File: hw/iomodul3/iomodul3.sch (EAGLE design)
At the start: 56 parts, among them IC1 MCP2551, IC3 STM32F042K, IC4 MCP1700T3302E/TT, IC5 DS8289, Q2 8MHz

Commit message: board version 3 begonnen
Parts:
- removed C10: 1µ 6,3V, schlager_passiv:C-EUC0805
- removed C11, C5: 12p, schlager_passiv:C-EUC0805
- removed C4: (no value), schlager_passiv:C-EUC0805
- removed C6: 10n, schlager_passiv:C-EUC0805
- removed C7, C9: 4µ7 6,3V, schlager_passiv:C-EUC0805
- removed C8: 100n, schlager_passiv:C-EUC0805
- removed IC3: STM32F042K, MYSGS:STM32F042
- removed JP3: (no value), pinhead:PINHD-1X6
- removed Q1: (no value), crystal:CRYSTALHC49U-V
- removed Q2: 8MHz, MYPASS:MT-CRYSTAL
- removed R4, R6, R9: (no value), schlager_passiv:R-EU_R0805
- added C20: 1uF, schlager_passiv:C-EUC0805
- added C21, C22, C26, C27: 100nF, schlager_passiv:C-EUC0805
- added C23, C24: 22p, schlager_passiv:C-EUC0805
- added CN2: PINHEAD-2x5-P1.27, Connettori:0171_PH127-205DF055G00A
- added IC2: SAMD21G18A-AUT, IntegratedCircuits:1792_SAMD21G18A-AUT
- added ICSP: 3x2 M, Connettori:0114_PH254-203DF118A00V
- added L6, L7: MH2029-300Y, Protezione:0001_BLM21PG300SN1D_/_MH2029-300Y
- added R15: 10k, schlager_passiv:R-EU_R0805
- added R18: 330R, schlager_passiv:R-EU_R0805
- added U$1: MCP2515-I/ST, CHIP_MCP:MCP2515-I/ST
- added USB2: MICRO-USB-AB1, Connettori:0631_MCR-AB1-S-RA-SMT-TR
- added Y1, Y4: 32,768Khz_SMD, Cristalli:0213_ABS07-32.768KHZ-T
- added Z5, Z6: CG0603MLC-05E, Protezione:0010_BRNCG0603MLC-05E
- C2, C3: value 100n -> 22p
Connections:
- removed net LED1: IC3G$1.PA5/AIN5, R5.2
- removed net N$5: C5.2, IC3G$1.PF0/OSC_IN, Q1.2, Q2G$1.2
- removed net NRST: IC3G$1./RST, JP3.5
- removed net PA1: IC3G$1.PA1/AIN1, SV1.5
- removed net PA10: IC3G$1.PA10, SV1.11
- removed net PA15: IC3G$1.PA15, SV1.12
- removed net PA2: IC3G$1.PA2/AIN2, SV1.6
- removed net PA3: IC3G$1.PA3/AIN3, SV1.18
- removed net PA6: IC3G$1.PA6/AIN6, SV1.7
- removed net PA7: IC3G$1.PA7/AIN7, SV1.8
- removed net PA8: IC3G$1.PA8, SV1.9
- removed net PA9: IC3G$1.PA9, SV1.10
- removed net PB3: IC3G$1.PB3/SPI1_SCK, SV1.13
- removed net PB4: IC3G$1.PB4/SPI1_MISO, SV1.14
- removed net PB5: IC3G$1.PB5/SPI1_MOSI, SV1.15
- removed net PB6: IC3G$1.PB6/I2C1_SCL, SV1.16
- removed net PB7: IC3G$1.PB7/I2C1_SDA, SV1.17
- removed net SWCLK: IC3G$1.PA14, JP3.2
- removed net SWDIO: IC3G$1.PA13, JP3.4
- removed net SWO: JP3.6
- removed net UIN: C4.1, IC3G$1.PA0/AIN0, R4.2, R6.1
- removed net VDD_TARGET: JP3.1
- new net #0_RX: IC2.PB23/EIC/SCOM5PAD3, SV1.17
- new net #11_MOSI: IC2.PA16/I2C/EIC/SCOM1PAD0+/TC2, SV1.15, U$1.SI
- new net #12_MISO: IC2.PA19/EIC/SCOM1PAD3+/TC3, SV1.14, U$1.SO
- new net #13_SCK: IC2.PA17/I2C/EIC/SCOM1PAD1+/TC2, SV1.13, U$1.SCK
- new net #1_TX: IC2.PB22/EIC/SCOM5PAD2, SV1.16
- new net #3_IO: IC2.PA9/I2C/EIC/AIN17/SCOM2PAD1+/TC0, SV1.9
- new net #9_CS_HEADER: IC2.PA7/EIC/AIN7/SCOM0PAD3/TC1, SV1.12
- new net #A0: IC2.PA2/EIC/AIN0, SV1.5
- new net #A1: IC2.PB8/EIC/AIN2/SCOM4PAD0/TC4, SV1.6
- new net #A2: IC2.PB9/EIC/AIN3/SCOM4PAD1//TC4, SV1.7
- new net #A3: IC2.PA4/EIC/REF/AIN4/SCOM0PAD0/TC0, SV1.8
- new net #A4: IC2.PA5/EIC/AIN5/SCOM0PAD1/TC0, SV1.18
- new net CS_MCP: IC2.PA18/EIC/SCOM1PAD2+/TC3, U$1.~CS
- new net DGI_GPIO0: IC2.PA13/I2C/EIC/SCOM2PAD1+/TC2
- new net DGI_GPIO1: IC2.PA21/EIC/SCOM5PAD3+
- new net DGI_GPIO2: IC2.PA6/EIC/AIN6/SCOM0PAD2/TC1
- new net MCPOSC1: C3.1, U$1.OSC1, Y1.1
- new net MCPOSC2: C2.1, U$1.OSC2, Y1.2
- new net PA00_XIN32: C23.2, IC2.PA0/XIN32/EIC/SCOM1PAD0/TC2, Y4.2
- new net PA01_XOUT32: C24.2, IC2.PA1/XOUT32/EIC/SCOM1PAD1/TC2, Y4.1
- new net PA03_AREFA: IC2.PA3/EIC/REF/AIN1
- new net PA08_TCC0-W0: IC2.PA8/I2C/AIN16/SCOM2PAD0+/TC0
- new net PA10_TCC0-W2: IC2.PA10/EIC/AIN18/SCOM2PAD2+/TC1
- new net PA11_TCC0-W3: IC2.PA11/EIC/AIN19/SCOM2PAD3+/TC1
- new net PA14_TCC0-W4: IC2.PA14/XIN/EIC/SCOM2PAD2+/TC3
- new net PA15_TCC0-W5: IC2.PA15/XOUT/EIC/SCOM2PAD3+/TC3
- new net PA20_TCC0-W6: IC2.PA20/EIC/SCOM5PAD2+
- new net PA27_TX_LED: IC2.PA27/EIC
- new net PA28_USB_HOST_EN: IC2.PA28/EIC
- new net PA30_SWCLK: CN2.4, IC2.PA30/EIC/SCOM1PAD2/TC1
- new net PA31_SWDIO1: CN2.2, IC2.PA31/EIC/SCOM1PAD3/TC1
- new net PB02_AIN10: IC2.PB2/EIC/AIN10/SCOM5PAD0
- new net PB03_RX_LED: IC2.PB3/EIC/AIN11/SCOM5PAD1
- new net PB10_S4_SPI_MOSI: IC2.PB10/EIC/SCOM4PAD2/TC5, ICSP.4
- new net PB11_S4_SPI_SCK: IC2.PB11/EIC/SCOM4PAD3/TC5, ICSP.3
- new net PB12_S4_SPI_MISO: IC2.PA12/I2C/EIC/SCOM2PAD0+/TC2, ICSP.1
- new net RESET: CN2.10, ICSP.5, R18.2
- new net SCL: IC2.PA23/I2C/EIC/SCOM5PAD1+/TC4, R2.1, SV1.10
- new net SDA: IC2.PA22/I2C/EIC/SCOM5PAD0+/TC4, R15.1, SV1.11
- new net TARGET_RESET_EDBG: IC2.RESETN, R18.1, U$1.~RESET
- new net TARGET_USB_N: IC2.PA24/EIC/SCOM3PAD2+/TC5, USB2.D-, Z6.1
- new net TARGET_USB_P: IC2.PA25/EIC/SCOM3PAD3+/TC5, USB2.D+, Z5.1
- new net VDDCORE: C20.1, IC2.VDDCORE1
- net +24V: no longer R4.1
- net +3V3: now also C21.1, C26.1, C27.2, CN2.1, IC2.VDDIN, IC2.VDDIO1, IC2.VDDIO2, L6.2, R15.2, R2.2; no longer C10.2, C2.2, C3.2, C6.2, C7.2, C9.2, IC3G$2.VCC, IC3G$2.VCC1, IC3G$2.VCCA
- net +5V: now also ICSP.2
- net CANRX: now also U$1.RXCAN; no longer IC3G$1.PA11/CAN_RX
- net CANTX: now also U$1.TXCAN; no longer IC3G$1.PA12/CAN_TX
- net GND: now also C2.2, C20.2, C21.2, C22.2, C23.1, C24.1, C26.2, C27.1, C3.2, CN2.3, CN2.5, CN2.9, IC2.GND1, IC2.GND2, IC2.GND3, IC2.GNDANA, ICSP.6, L7.2, USB2.UGND, Z5.2, Z6.2; no longer C10.1, C11.1, C2.1, C3.1, C4.2, C5.1, C6.1, C7.1, C8.2, C9.1, IC3G$2.GND, IC3G$2.GND1, JP3.3, Q2G$2.GND, Q2G$3.GND, R2.2, R6.2, R9.2
- net LED2: no longer IC3G$1.PA4/AIN4
- net LED3_: no longer IC3G$1.PB0/AIN8
- net LED4_: no longer IC3G$1.BP1/AIN9
- net N$15: now also C22.1, IC2.VDDANA, L6.1; no longer IC3G$1.PB8/BOOT0, R2.1
- net N$4: now also L7.1, USB2.G1, USB2.G10, USB2.G11, USB2.G2, USB2.G3, USB2.G4, USB2.G5, USB2.G6, USB2.G7, USB2.G8, USB2.G9, USB2.SH1, USB2.SH2, USB2.SH3, USB2.SH4; no longer C11.2, IC3G$1.PF1/OSC_OUT, Q1.1, Q2G$1.1
- net PE: no longer C8.1, CON2G$2.FGND, R9.1
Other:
- note added: "USB AB"
- moved on the sheet: BR1, BR2, C1, C12, C2, C3, CON1G$1, CON2G$1, IC1, JP1, JP2, LED1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

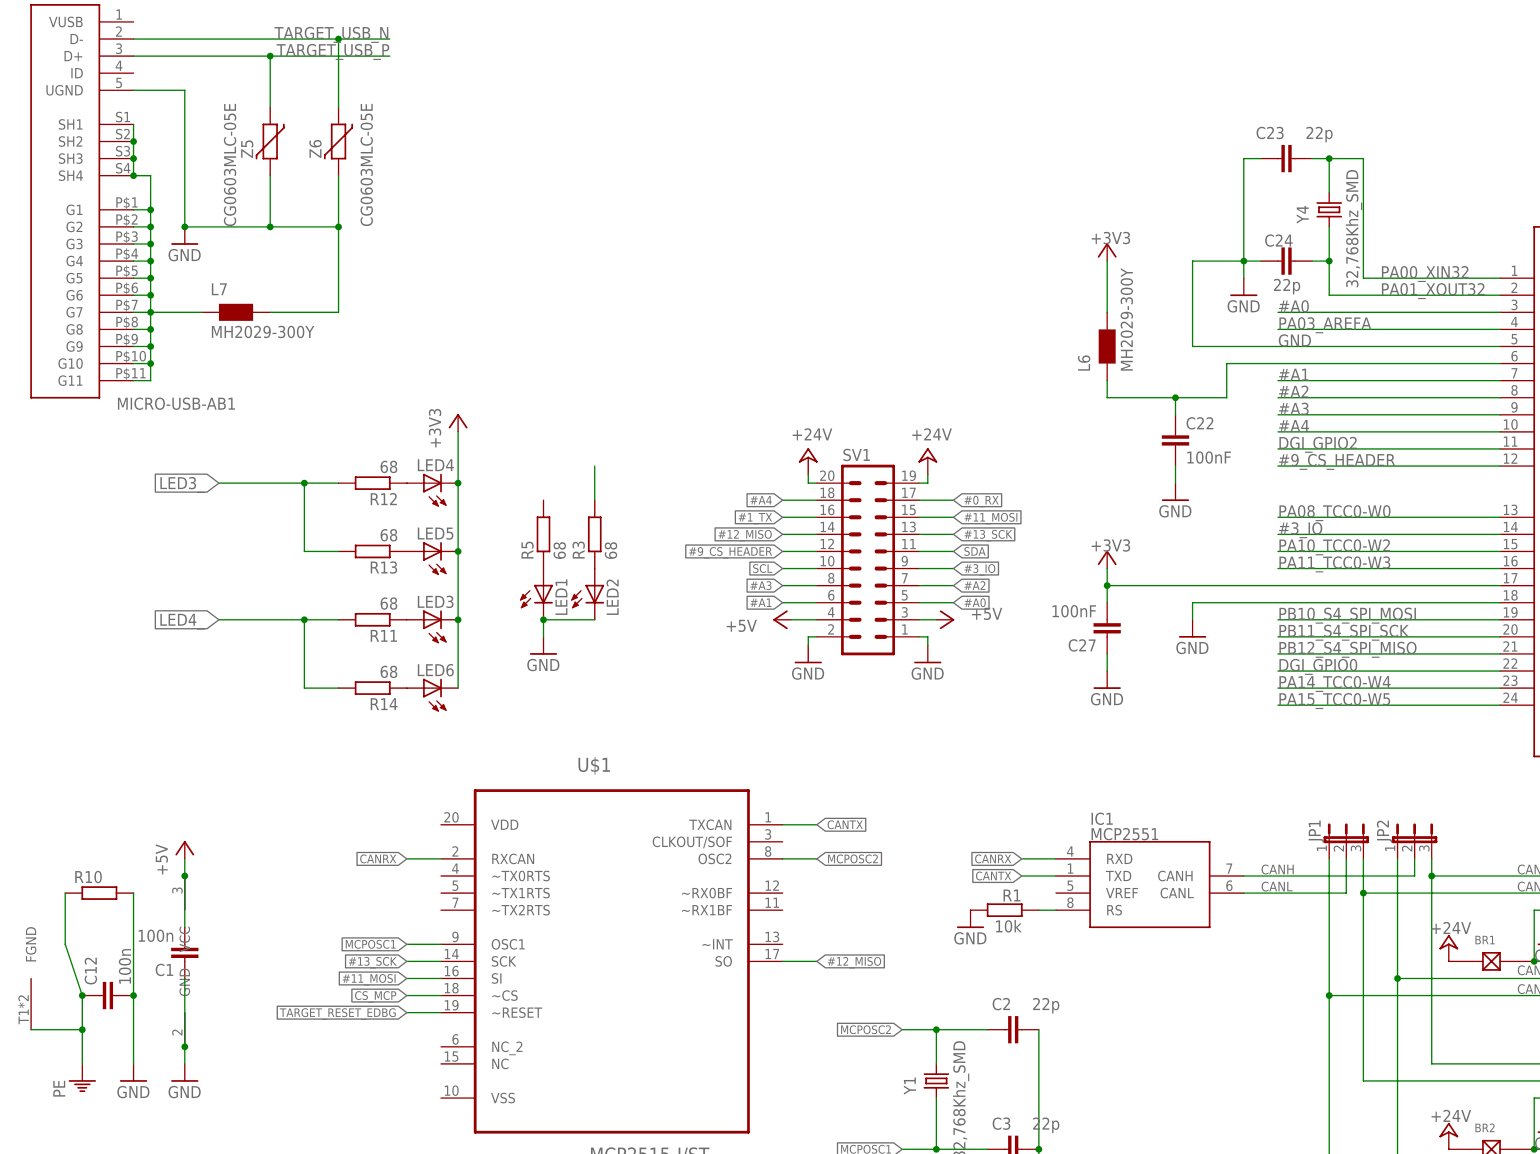
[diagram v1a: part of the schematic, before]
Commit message: mod of CANable USB to CAN modul
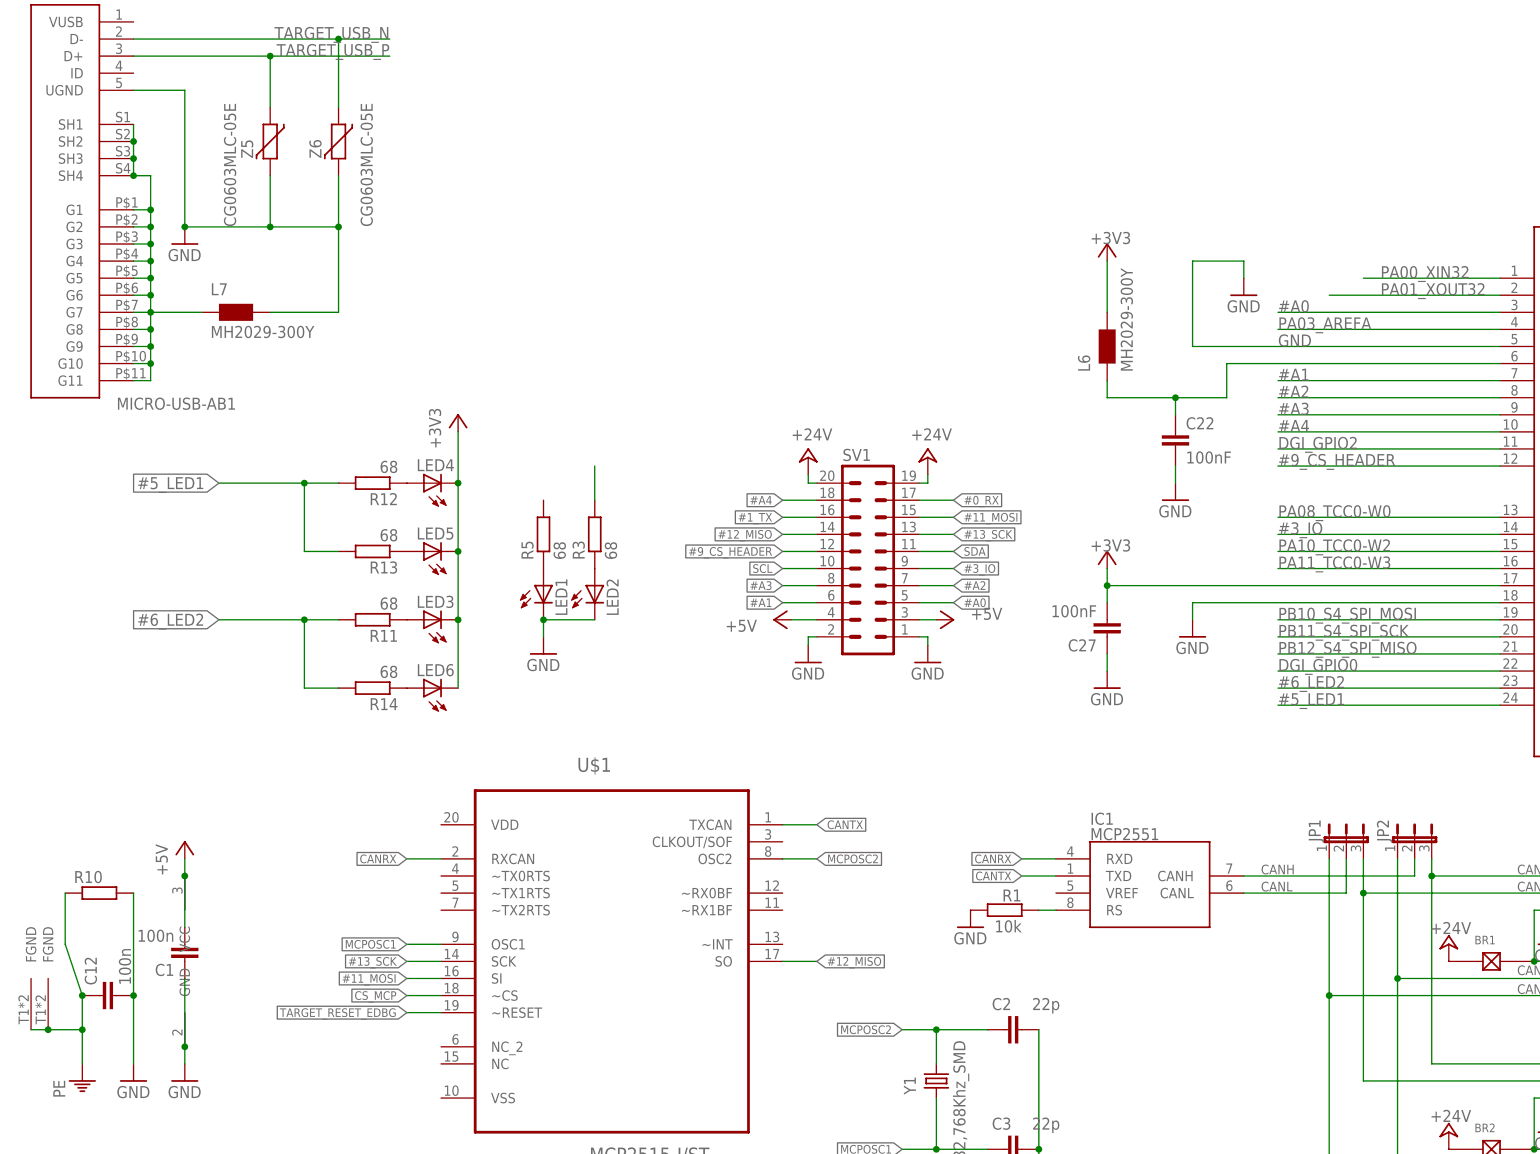
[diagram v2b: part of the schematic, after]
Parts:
- removed C23, C24: 22p, schlager_passiv:C-EUC0805
- removed Y4: 32,768Khz_SMD, Cristalli:0213_ABS07-32.768KHZ-T
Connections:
- removed net LED3_: R12.2, R13.2
- removed net LED4_: R11.2, R14.2
- removed net PA14_TCC0-W4: IC2.PA14/XIN/EIC/SCOM2PAD2+/TC3
- removed net PA15_TCC0-W5: IC2.PA15/XOUT/EIC/SCOM2PAD3+/TC3
- new net #5_LED1: IC2.PA15/XOUT/EIC/SCOM2PAD3+/TC3, R12.2, R13.2
- new net #6_LED2: IC2.PA14/XIN/EIC/SCOM2PAD2+/TC3, R11.2, R14.2
- net GND: no longer C23.1, C24.1
- net PA00_XIN32: no longer C23.2, Y4.2
- net PA01_XOUT32: no longer C24.2, Y4.1
- net PE: now also CON2G$2.FGND
